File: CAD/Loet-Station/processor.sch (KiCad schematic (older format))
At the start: 0 parts

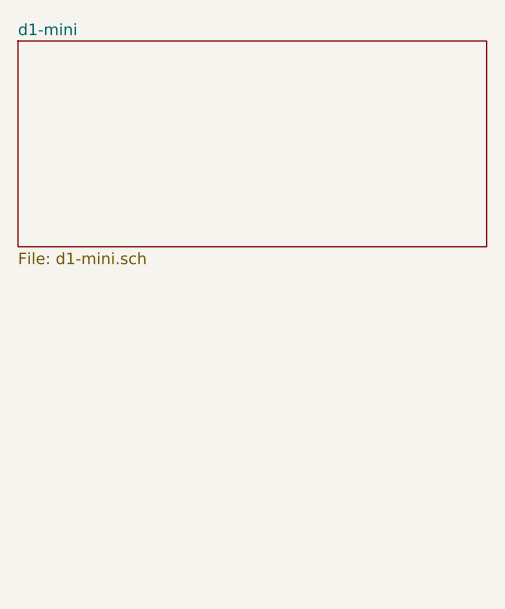
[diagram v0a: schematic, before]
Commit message: updated schematics
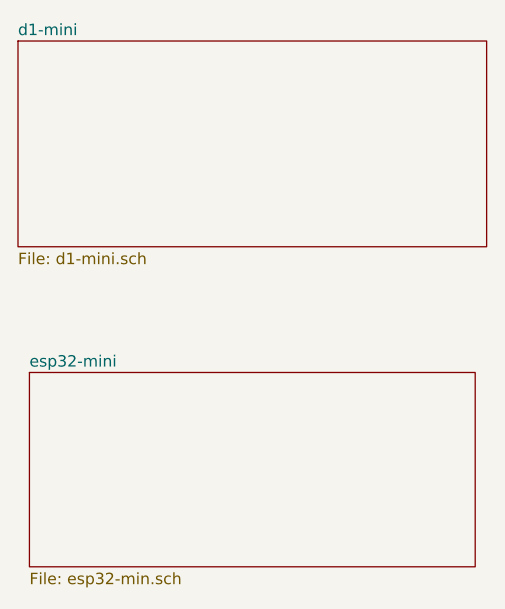
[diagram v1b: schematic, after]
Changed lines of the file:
@@
 $Descr A4 11693 8268
 encoding utf-8
-Sheet 2 6
+Sheet 2 7
 Title ""
 Date ""
@@
 F1 "d1-mini.sch" 50
 $EndSheet
+$Sheet
+S 6900 2500 1950 850
+U 605387CE
+F0 "esp32-mini" 50
+F1 "esp32-min.sch" 50
+$EndSheet
 $EndSCHEMATC
